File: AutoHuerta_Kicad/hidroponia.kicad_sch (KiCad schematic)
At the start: 37 parts, among them J1 bornera, J2 bornera, J3 Barrel_Jack, J4 pin, J5 Conn_01x08_Pin, J6 Pin, K1 RELAY, Q1 BC817, Q2 BS170F, Q3 BC817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

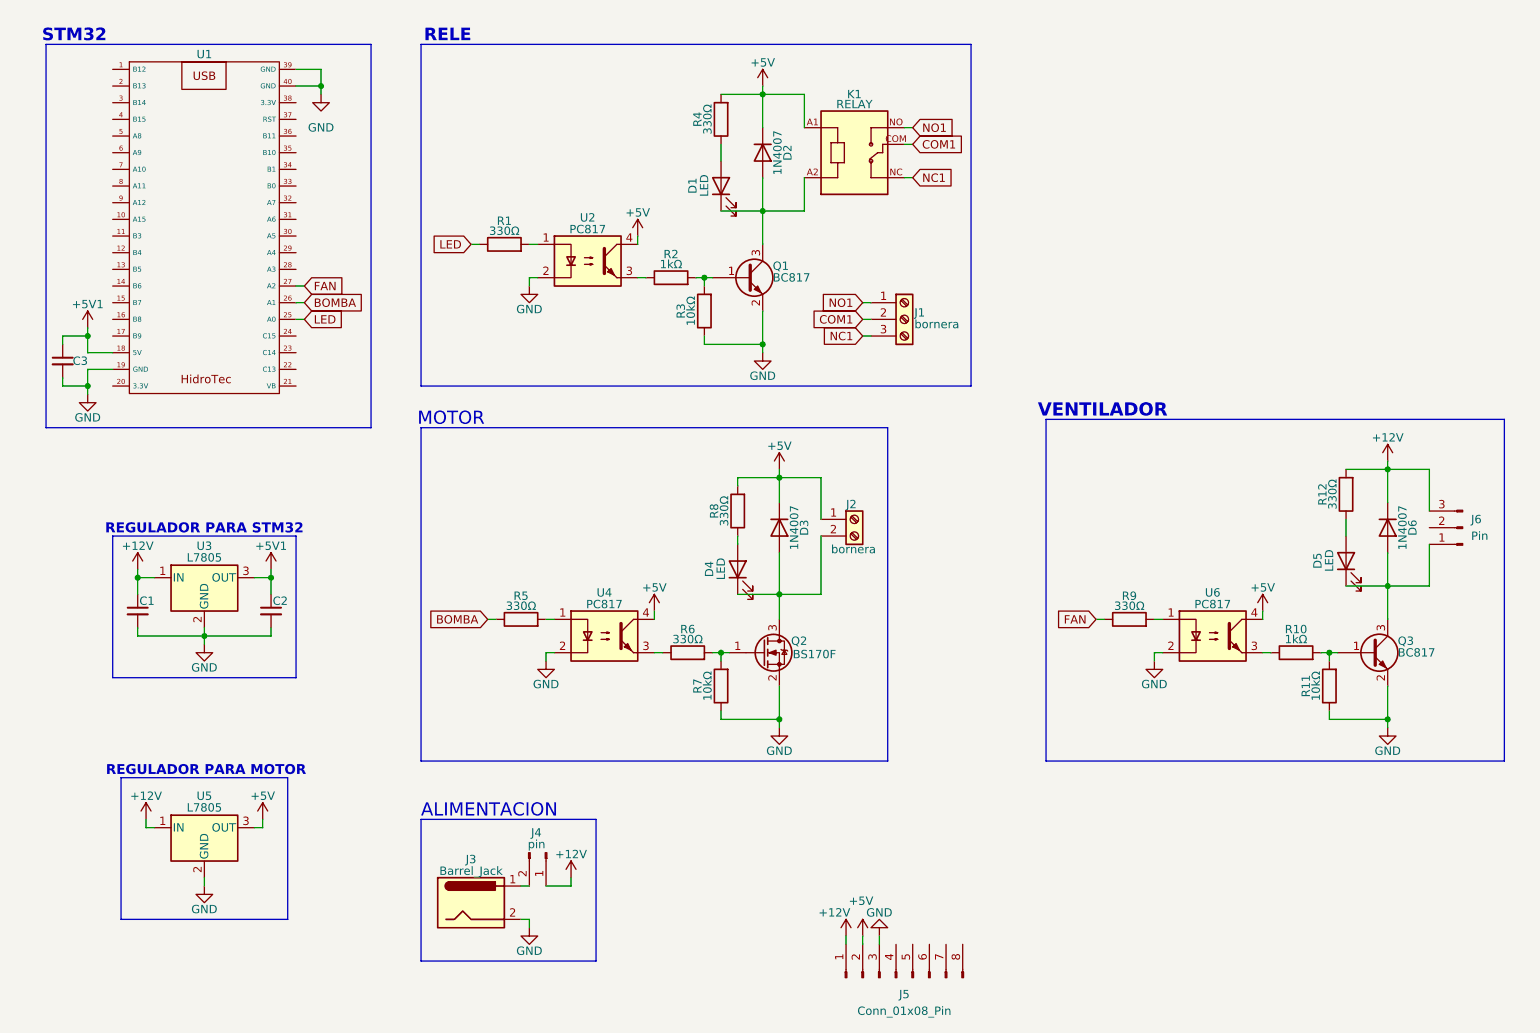
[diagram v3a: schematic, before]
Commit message: Esquematico terminado
Terminamos de corregir y agregar cosas al esquematico y empezamos a acomodar los componentes en el pcb
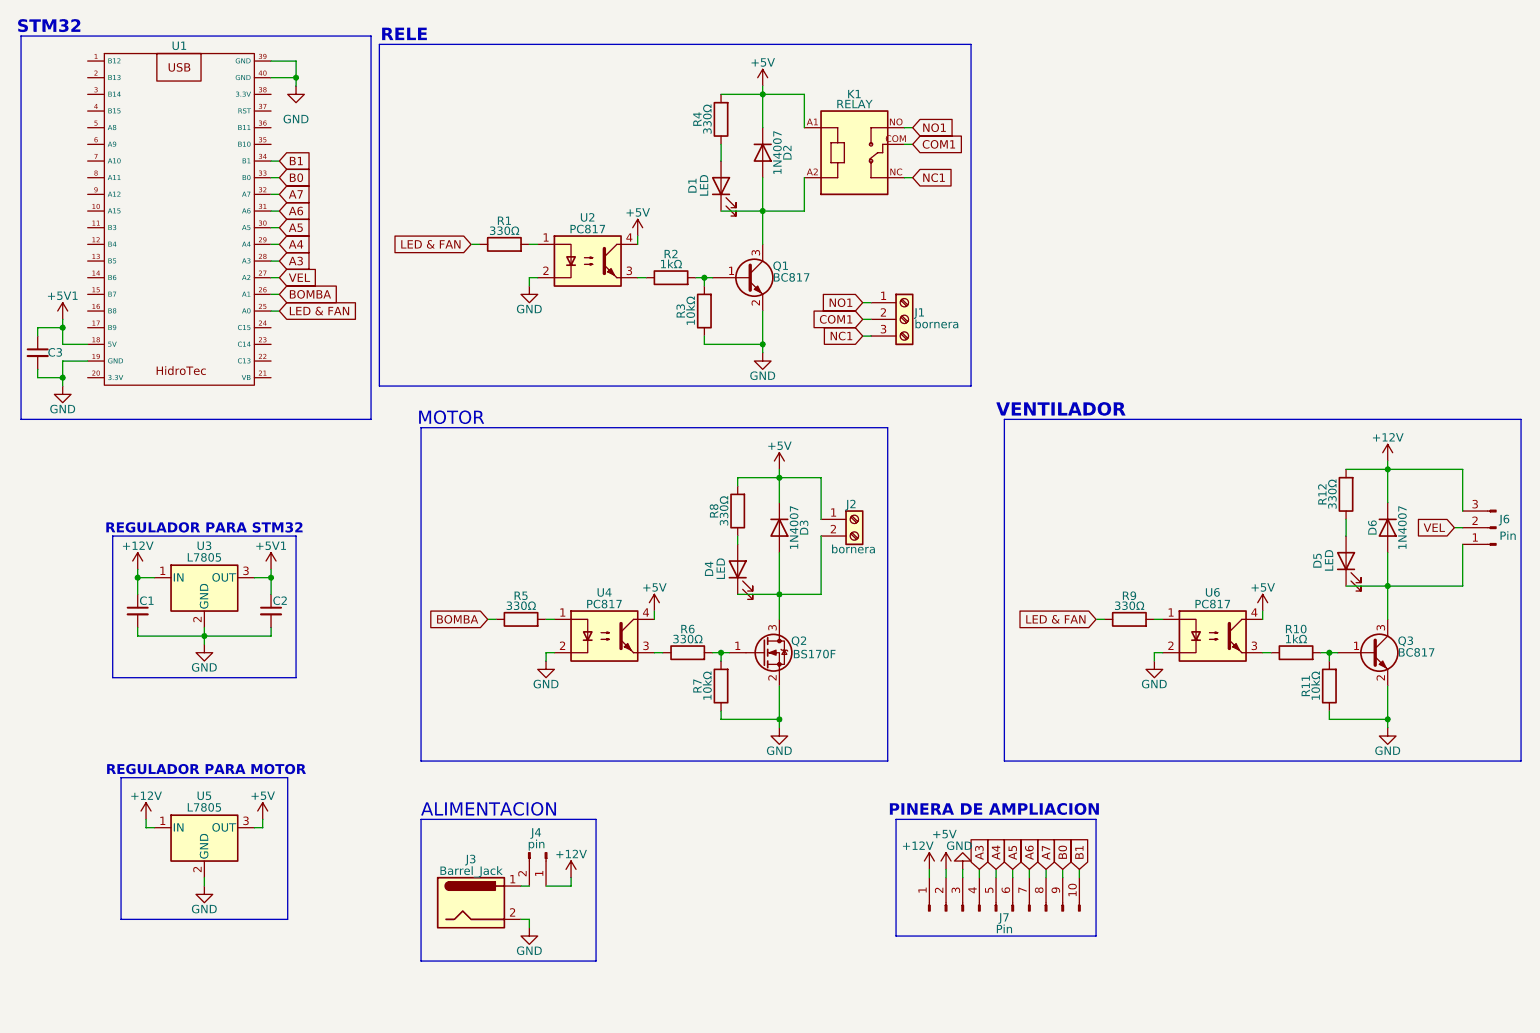
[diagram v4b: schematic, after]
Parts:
- removed J5: Conn_01x08_Pin, symbol Connector:Conn_01x08_Pin
- added J7: Pin, Connector_IDC:IDC-Header_2x05-1MP_P2.54mm_Latch6.5mm_Vertical, symbol Connector:Conn_01x10_Pin
- U1: footprint huella de stm32:stm32 -> Huellas:stm32
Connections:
- net LED is gone; now on net LED & FAN: R1.1, U1.25 (A0)
- net +12V: now also J7.1 (Pin_1)
- net +5V: now also J7.2 (Pin_2)
- net GND: now also J7.3 (Pin_3)
- net VEL: now reaches J6.2 (Pin_2)
- net VEL: now also U1.27 (A2)
- net A3: now reaches U1.28 (A3)
- net A3: now also J7.4 (Pin_4)
- net A4: now reaches U1.29 (A4)
- net A4: now also J7.5 (Pin_5)
- net A5: now reaches U1.30 (A5)
- net A5: now also J7.6 (Pin_6)
- net A6: now reaches U1.31 (A6)
- net A6: now also J7.7 (Pin_7)
- net A7: now reaches U1.32 (A7)
- net A7: now also J7.8 (Pin_8)
- net B0: now reaches U1.33 (B0)
- net B0: now also J7.9 (Pin_9)
- net B1: now reaches U1.34 (B1)
- net B1: now also J7.10 (Pin_10)
- net FAN renamed LED & FAN
- net LED & FAN: no longer U1.27 (A2)
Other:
- note added: "PINERA DE AMPLIACION"
- moved on the sheet: C3, J6, U1

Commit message: PCB
Acomodamos un poco el PCB y cambiamos pines de lugar
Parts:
- R12: value 330Ω -> 1kΩ
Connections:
- net +12V: now also J7.2 (Pin_2); no longer J7.1 (Pin_1)
- net +5V: now also J7.3 (Pin_3); no longer J7.2 (Pin_2)
- net GND: now also J7.1 (Pin_1); no longer J7.3 (Pin_3)
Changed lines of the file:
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@@
 	(wire
 		(pts
+			(xy 153.67 143.51) (xy 153.67 144.78)
+		)
+		(stroke
+			(width 0)
+			(type default)
+		)
+	)
+	(wire
+		(pts
 			(xy 232.41 93.98) (xy 232.41 100.33)
 		)
@@
 	(wire
 		(pts
+			(xy 151.13 143.51) (xy 151.13 144.78)
+		)
+		(stroke
+			(width 0)
+			(type default)
+		)
+	)
+	(wire
+		(pts
 			(xy 50.8 58.42) (xy 52.07 58.42)
 		)
@@
 		)
 	)
-	(wire
-		(pts
-			(xy 151.13 143.51) (xy 151.13 144.78)
-		)
-		(stroke
-			(width 0)
-			(type default)
-		)
-	)
 	(bus
 		(pts
@@
 	(wire
 		(pts
-			(xy 153.67 143.51) (xy 153.67 144.78)
-		)
-		(stroke
-			(width 0)
-			(type default)
-		)
-	)
-	(wire
-		(pts
 			(xy 92.71 110.49) (xy 92.71 111.76)
 		)
@@
 	(wire
 		(pts
-			(xy 156.21 143.51) (xy 156.21 144.78)
-		)
-		(stroke
-			(width 0)
-			(type default)
-		)
-	)
-	(wire
-		(pts
 			(xy 128.27 101.6) (xy 128.27 105.41)
 		)
@@
 	(wire
 		(pts
+			(xy 156.21 143.51) (xy 156.21 144.78)
+		)
+		(stroke
+			(width 0)
+			(type default)
+		)
+	)
+	(wire
+		(pts
 			(xy 116.84 63.5) (xy 125.73 63.5)
 		)
@@
 			)
 		)
-		(property "Value" "330Ω"
+		(property "Value" "1kΩ"
 			(at 212.598 86.36 90)
 			(effects
@@
 	(symbol
 		(lib_id "power:+12V")
-		(at 151.13 143.51 0)
+		(at 153.67 143.51 0)
 		(unit 1)
 		(exclude_from_sim no)
@@
 		(dnp no)
 		(property "Reference" "#PWR027"
-			(at 151.13 147.32 0)
+			(at 153.67 147.32 0)
 			(effects
 				(font
@@
 		)
 		(property "Value" "+12V"
-			(at 149.352 139.954 0)
+			(at 153.416 137.16 0)
 			(effects
 				(font
@@
 		)
 		(property "Footprint" ""
-			(at 151.13 143.51 0)
+			(at 153.67 143.51 0)
 			(effects
 				(font
@@
 		)
 		(property "Datasheet" ""
-			(at 151.13 143.51 0)
+			(at 153.67 143.51 0)
 			(effects
 				(font
@@
 		)
 		(property "Description" "Power symbol creates a global label with name \"+12V\""
-			(at 151.13 143.51 0)
+			(at 153.67 143.51 0)
 			(effects
 				(font
@@
 	(symbol
 		(lib_id "power:+5V")
-		(at 153.67 143.51 0)
+		(at 156.21 143.51 0)
 		(unit 1)
 		(exclude_from_sim no)
@@
 		(dnp no)
 		(property "Reference" "#PWR028"
-			(at 153.67 147.32 0)
+			(at 156.21 147.32 0)
 			(effects
 				(font
@@
 		)
 		(property "Value" "+5V"
-			(at 153.416 138.176 0)
+			(at 156.21 138.43 0)
 			(effects
 				(font
@@
 		)
 		(property "Footprint" ""
-			(at 153.67 143.51 0)
+			(at 156.21 143.51 0)
 			(effects
 				(font
@@
 		)
 		(property "Datasheet" ""
-			(at 153.67 143.51 0)
+			(at 156.21 143.51 0)
 			(effects
 				(font
@@
 		)
 		(property "Description" "Power symbol creates a global label with name \"+5V\""
-			(at 153.67 143.51 0)
+			(at 156.21 143.51 0)
 			(effects
 				(font
@@
 	(symbol
 		(lib_id "power:GND")
-		(at 156.21 143.51 180)
+		(at 151.13 143.51 180)
 		(unit 1)
 		(exclude_from_sim no)
@@
 		(dnp no)
 		(property "Reference" "#PWR029"
-			(at 156.21 137.16 0)
+			(at 151.13 137.16 0)
 			(effects
 				(font
@@
 		)
 		(property "Value" "GND"
-			(at 155.702 139.954 0)
+			(at 150.622 139.954 0)
 			(effects
 				(font
@@
 		)
 		(property "Footprint" ""
-			(at 156.21 143.51 0)
+			(at 151.13 143.51 0)
 			(effects
 				(font
@@
 		)
 		(property "Datasheet" ""
-			(at 156.21 143.51 0)
+			(at 151.13 143.51 0)
 			(effects
 				(font
@@
 		)
 		(property "Description" "Power symbol creates a global label with name \"GND\" , ground"
-			(at 156.21 143.51 0)
+			(at 151.13 143.51 0)
 			(effects
 				(font

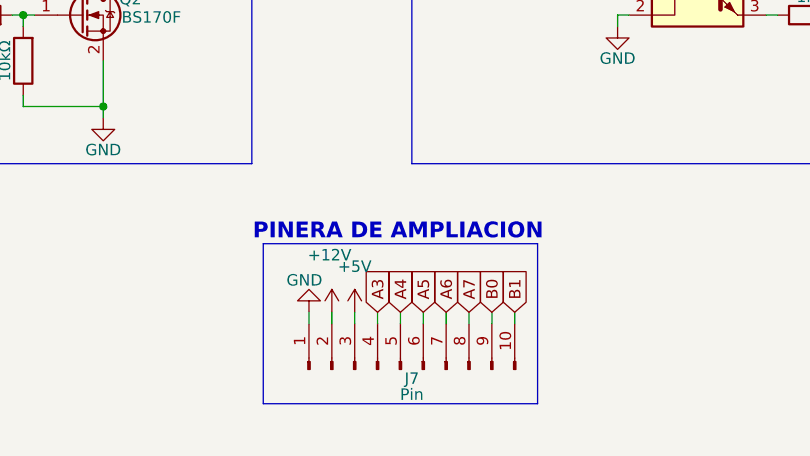
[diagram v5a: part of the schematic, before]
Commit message: PCB
PCB casi terminado, y cambiamos unas cosas del esquematico
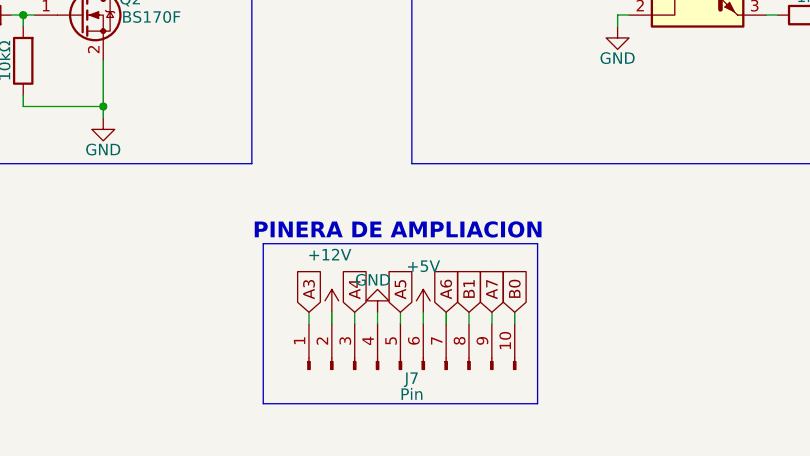
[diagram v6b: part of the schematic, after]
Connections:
- net +5V: now also J7.6 (Pin_6); no longer J7.3 (Pin_3)
- net A3: now also J7.1 (Pin_1); no longer J7.4 (Pin_4)
- net A4: now also J7.3 (Pin_3); no longer J7.5 (Pin_5)
- net A5: now also J7.5 (Pin_5); no longer J7.6 (Pin_6)
- net A7: now also J7.9 (Pin_9); no longer J7.8 (Pin_8)
- net B0: now also J7.10 (Pin_10); no longer J7.9 (Pin_9)
- net B1: now also J7.8 (Pin_8); no longer J7.10 (Pin_10)
- net GND: now also J7.4 (Pin_4); no longer J7.1 (Pin_1)
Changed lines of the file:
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@@
 		)
 	)
-	(wire
-		(pts
-			(xy 158.75 143.51) (xy 158.75 144.78)
-		)
-		(stroke
-			(width 0)
-			(type default)
-		)
-	)
 	(bus
 		(pts
@@
 		)
 	)
-	(wire
-		(pts
-			(xy 163.83 143.51) (xy 163.83 144.78)
-		)
-		(stroke
-			(width 0)
-			(type default)
-		)
-	)
 	(bus
 		(pts
@@
 		)
 	)
+	(wire
+		(pts
+			(xy 151.13 143.51) (xy 151.13 144.78)
+		)
+		(stroke
+			(width 0)
+			(type default)
+		)
+	)
 	(bus
 		(pts
@@
 	(wire
 		(pts
-			(xy 168.91 143.51) (xy 168.91 144.78)
+			(xy 173.99 143.51) (xy 173.99 144.78)
 		)
 		(stroke
@@
 	(wire
 		(pts
-			(xy 151.13 143.51) (xy 151.13 144.78)
-		)
-		(stroke
-			(width 0)
-			(type default)
-		)
-	)
-	(wire
-		(pts
 			(xy 50.8 58.42) (xy 52.07 58.42)
 		)
@@
 	(wire
 		(pts
+			(xy 161.29 143.51) (xy 161.29 144.78)
+		)
+		(stroke
+			(width 0)
+			(type default)
+		)
+	)
+	(wire
+		(pts
 			(xy 15.24 62.23) (xy 15.24 60.96)
 		)
@@
 	(wire
 		(pts
+			(xy 168.91 143.51) (xy 168.91 144.78)
+		)
+		(stroke
+			(width 0)
+			(type default)
+		)
+	)
+	(wire
+		(pts
 			(xy 121.92 101.6) (xy 128.27 101.6)
 		)
@@
 	(wire
 		(pts
-			(xy 173.99 143.51) (xy 173.99 144.78)
+			(xy 128.27 82.55) (xy 128.27 83.82)
 		)
 		(stroke
@@
 	(wire
 		(pts
-			(xy 128.27 82.55) (xy 128.27 83.82)
+			(xy 171.45 143.51) (xy 171.45 144.78)
 		)
 		(stroke
@@
 	(wire
 		(pts
-			(xy 171.45 143.51) (xy 171.45 144.78)
+			(xy 30.48 97.79) (xy 30.48 99.06)
 		)
 		(stroke
@@
 	(wire
 		(pts
-			(xy 30.48 97.79) (xy 30.48 99.06)
+			(xy 158.75 143.51) (xy 158.75 144.78)
 		)
 		(stroke
@@
 	(wire
 		(pts
-			(xy 50.8 55.88) (xy 52.07 55.88)
+			(xy 156.21 143.51) (xy 156.21 144.78)
 		)
 		(stroke
@@
 	(wire
 		(pts
-			(xy 161.29 143.51) (xy 161.29 144.78)
+			(xy 50.8 55.88) (xy 52.07 55.88)
 		)
 		(stroke
@@
 	(wire
 		(pts
-			(xy 118.11 110.49) (xy 119.38 110.49)
+			(xy 163.83 143.51) (xy 163.83 144.78)
 		)
 		(stroke
@@
 		)
 	)
-	(bus
+	(wire
 		(pts
-			(xy 26.67 92.71) (xy 54.61 92.71)
+			(xy 118.11 110.49) (xy 119.38 110.49)
 		)
 		(stroke
@@
 		)
 	)
-	(wire
+	(bus
 		(pts
-			(xy 156.21 143.51) (xy 156.21 144.78)
+			(xy 26.67 92.71) (xy 54.61 92.71)
 		)
 		(stroke
@@
 	(global_label "A7"
 		(shape input)
-		(at 168.91 143.51 90)
+		(at 171.45 143.51 90)
 		(fields_autoplaced yes)
 		(effects
@@
 		)
 		(property "Intersheetrefs" "${INTERSHEET_REFS}"
-			(at 168.91 138.2267 90)
+			(at 171.45 138.2267 90)
 			(effects
 				(font
@@
 	(global_label "B0"
 		(shape input)
-		(at 171.45 143.51 90)
+		(at 173.99 143.51 90)
 		(fields_autoplaced yes)
 		(effects
@@
 		)
 		(property "Intersheetrefs" "${INTERSHEET_REFS}"
-			(at 171.45 138.0453 90)
+			(at 173.99 138.0453 90)
 			(effects
 				(font
@@
 	(global_label "B1"
 		(shape input)
-		(at 173.99 143.51 90)
+		(at 168.91 143.51 90)
 		(fields_autoplaced yes)
 		(effects
@@
 		)
 		(property "Intersheetrefs" "${INTERSHEET_REFS}"
-			(at 173.99 138.0453 90)
+			(at 168.91 138.0453 90)
 			(effects
 				(font
@@
 	(global_label "A3"
 		(shape input)
-		(at 158.75 143.51 90)
+		(at 151.13 143.51 90)
 		(fields_autoplaced yes)
 		(effects
@@
 		)
 		(property "Intersheetrefs" "${INTERSHEET_REFS}"
-			(at 158.75 138.2267 90)
+			(at 151.13 138.2267 90)
 			(effects
 				(font
@@
 	(global_label "A4"
 		(shape input)
-		(at 161.29 143.51 90)
+		(at 156.21 143.51 90)
 		(fields_autoplaced yes)
 		(effects
@@
 		)
 		(property "Intersheetrefs" "${INTERSHEET_REFS}"
-			(at 161.29 138.2267 90)
+			(at 156.21 138.2267 90)
 			(effects
 				(font
@@
 	(global_label "A5"
 		(shape input)
-		(at 163.83 143.51 90)
+		(at 161.29 143.51 90)
 		(fields_autoplaced yes)
 		(effects
@@
 		)
 		(property "Intersheetrefs" "${INTERSHEET_REFS}"
-			(at 163.83 138.2267 90)
+			(at 161.29 138.2267 90)
 			(effects
 				(font
@@
 	(symbol
 		(lib_id "power:+5V")
-		(at 156.21 143.51 0)
+		(at 163.83 143.51 0)
 		(unit 1)
 		(exclude_from_sim no)
@@
 		(dnp no)
 		(property "Reference" "#PWR028"
-			(at 156.21 147.32 0)
+			(at 163.83 147.32 0)
 			(effects
 				(font
@@
 		)
 		(property "Value" "+5V"
-			(at 156.21 138.43 0)
+			(at 163.83 138.43 0)
 			(effects
 				(font
@@
 		)
 		(property "Footprint" ""
-			(at 156.21 143.51 0)
+			(at 163.83 143.51 0)
 			(effects
 				(font
@@
 		)
 		(property "Datasheet" ""
-			(at 156.21 143.51 0)
+			(at 163.83 143.51 0)
 			(effects
 				(font
@@
 		)
 		(property "Description" "Power symbol creates a global label with name \"+5V\""
-			(at 156.21 143.51 0)
+			(at 163.83 143.51 0)
 			(effects
 				(font
@@
 	(symbol
 		(lib_id "power:GND")
-		(at 151.13 143.51 180)
+		(at 158.75 143.51 180)
 		(unit 1)
 		(exclude_from_sim no)
@@
 		(dnp no)
 		(property "Reference" "#PWR029"
-			(at 151.13 137.16 0)
+			(at 158.75 137.16 0)
 			(effects
 				(font
@@
 		)
 		(property "Value" "GND"
-			(at 150.622 139.954 0)
+			(at 158.242 139.954 0)
 			(effects
 				(font
@@
 		)
 		(property "Footprint" ""
-			(at 151.13 143.51 0)
+			(at 158.75 143.51 0)
 			(effects
 				(font
@@
 		)
 		(property "Datasheet" ""
-			(at 151.13 143.51 0)
+			(at 158.75 143.51 0)
 			(effects
 				(font
@@
 		)
 		(property "Description" "Power symbol creates a global label with name \"GND\" , ground"
-			(at 151.13 143.51 0)
+			(at 158.75 143.51 0)
 			(effects
 				(font
